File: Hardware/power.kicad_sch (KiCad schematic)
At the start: 13 parts, among them J3 USB_C_Receptacle, U2 ADP2164ACPZ-3.3-R7

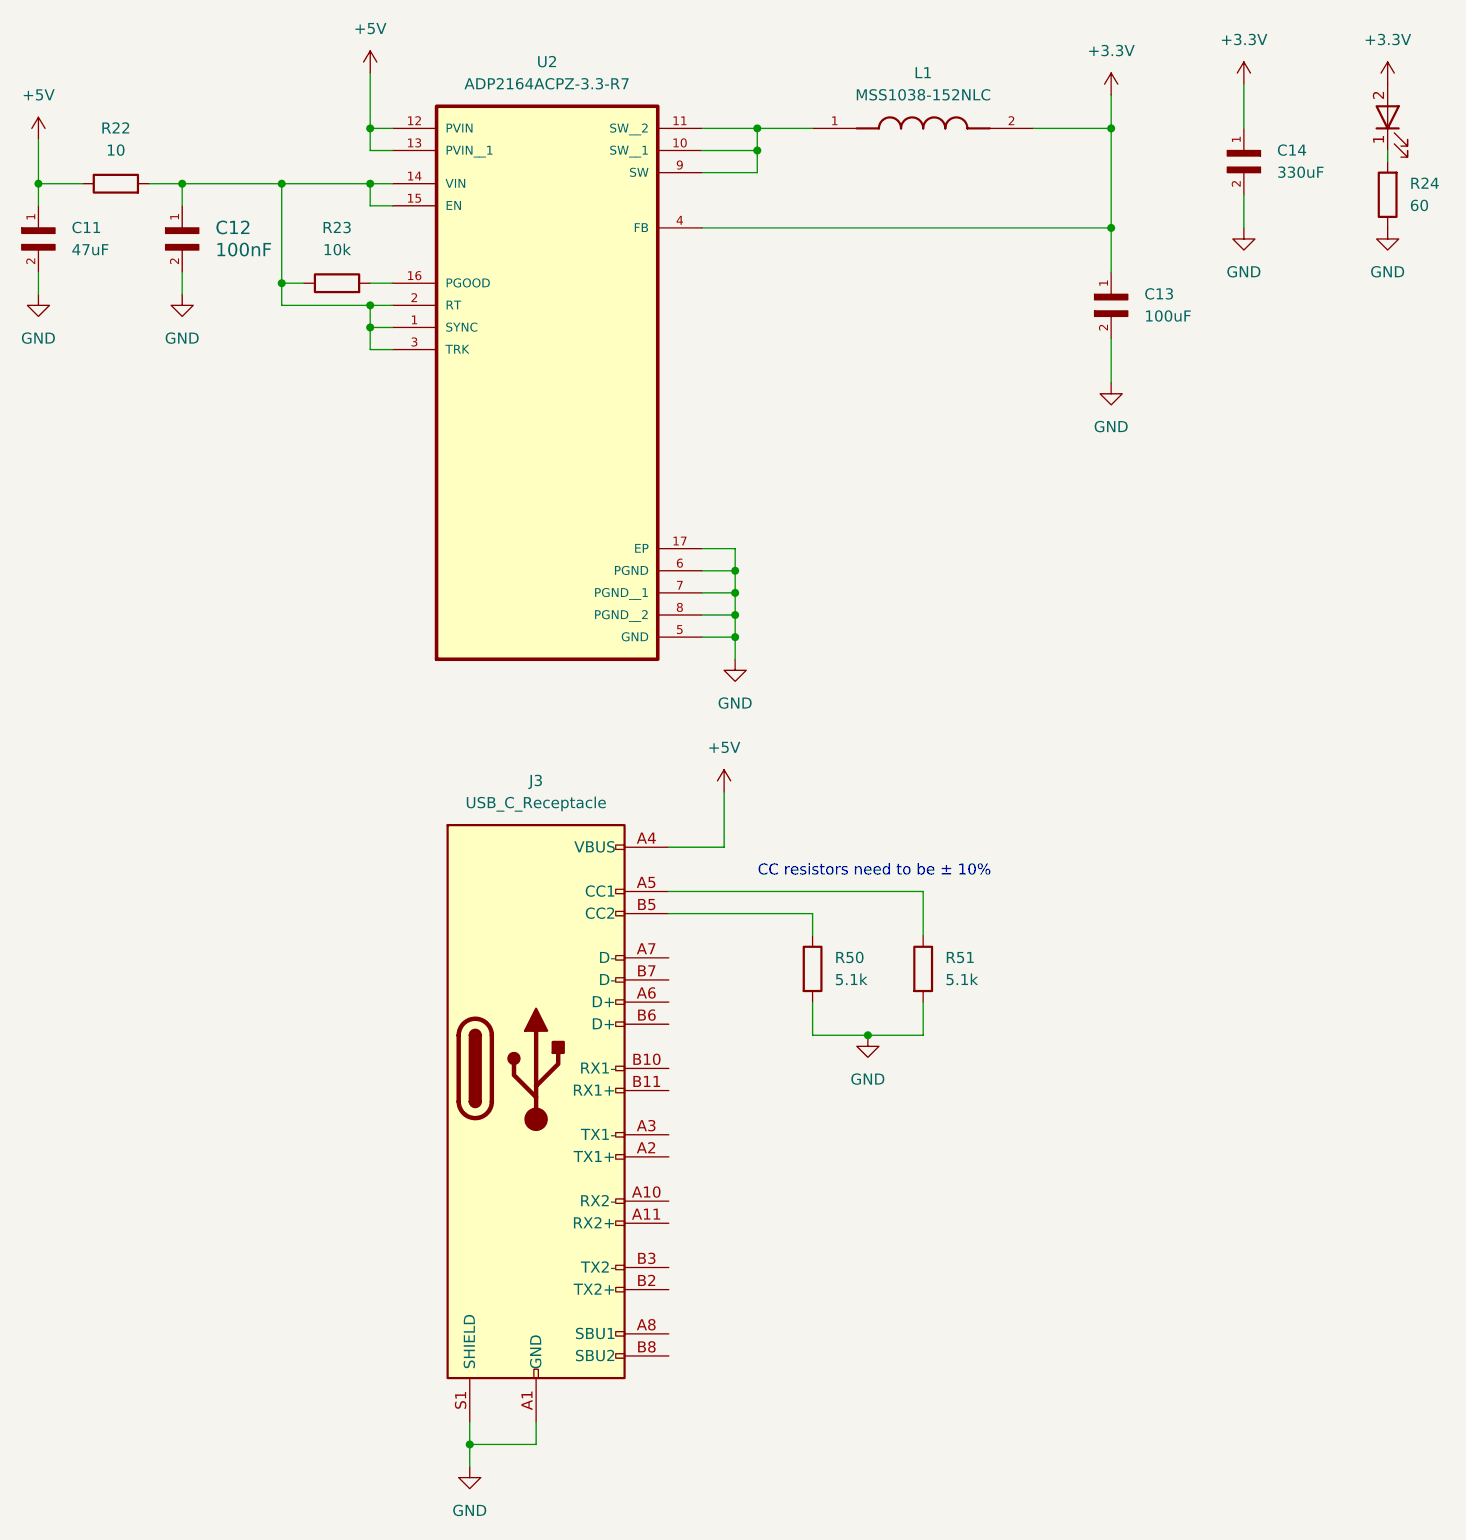
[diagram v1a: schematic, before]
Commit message: changed to SI4468, added 30 MHz oscillators, and connected it to MCU
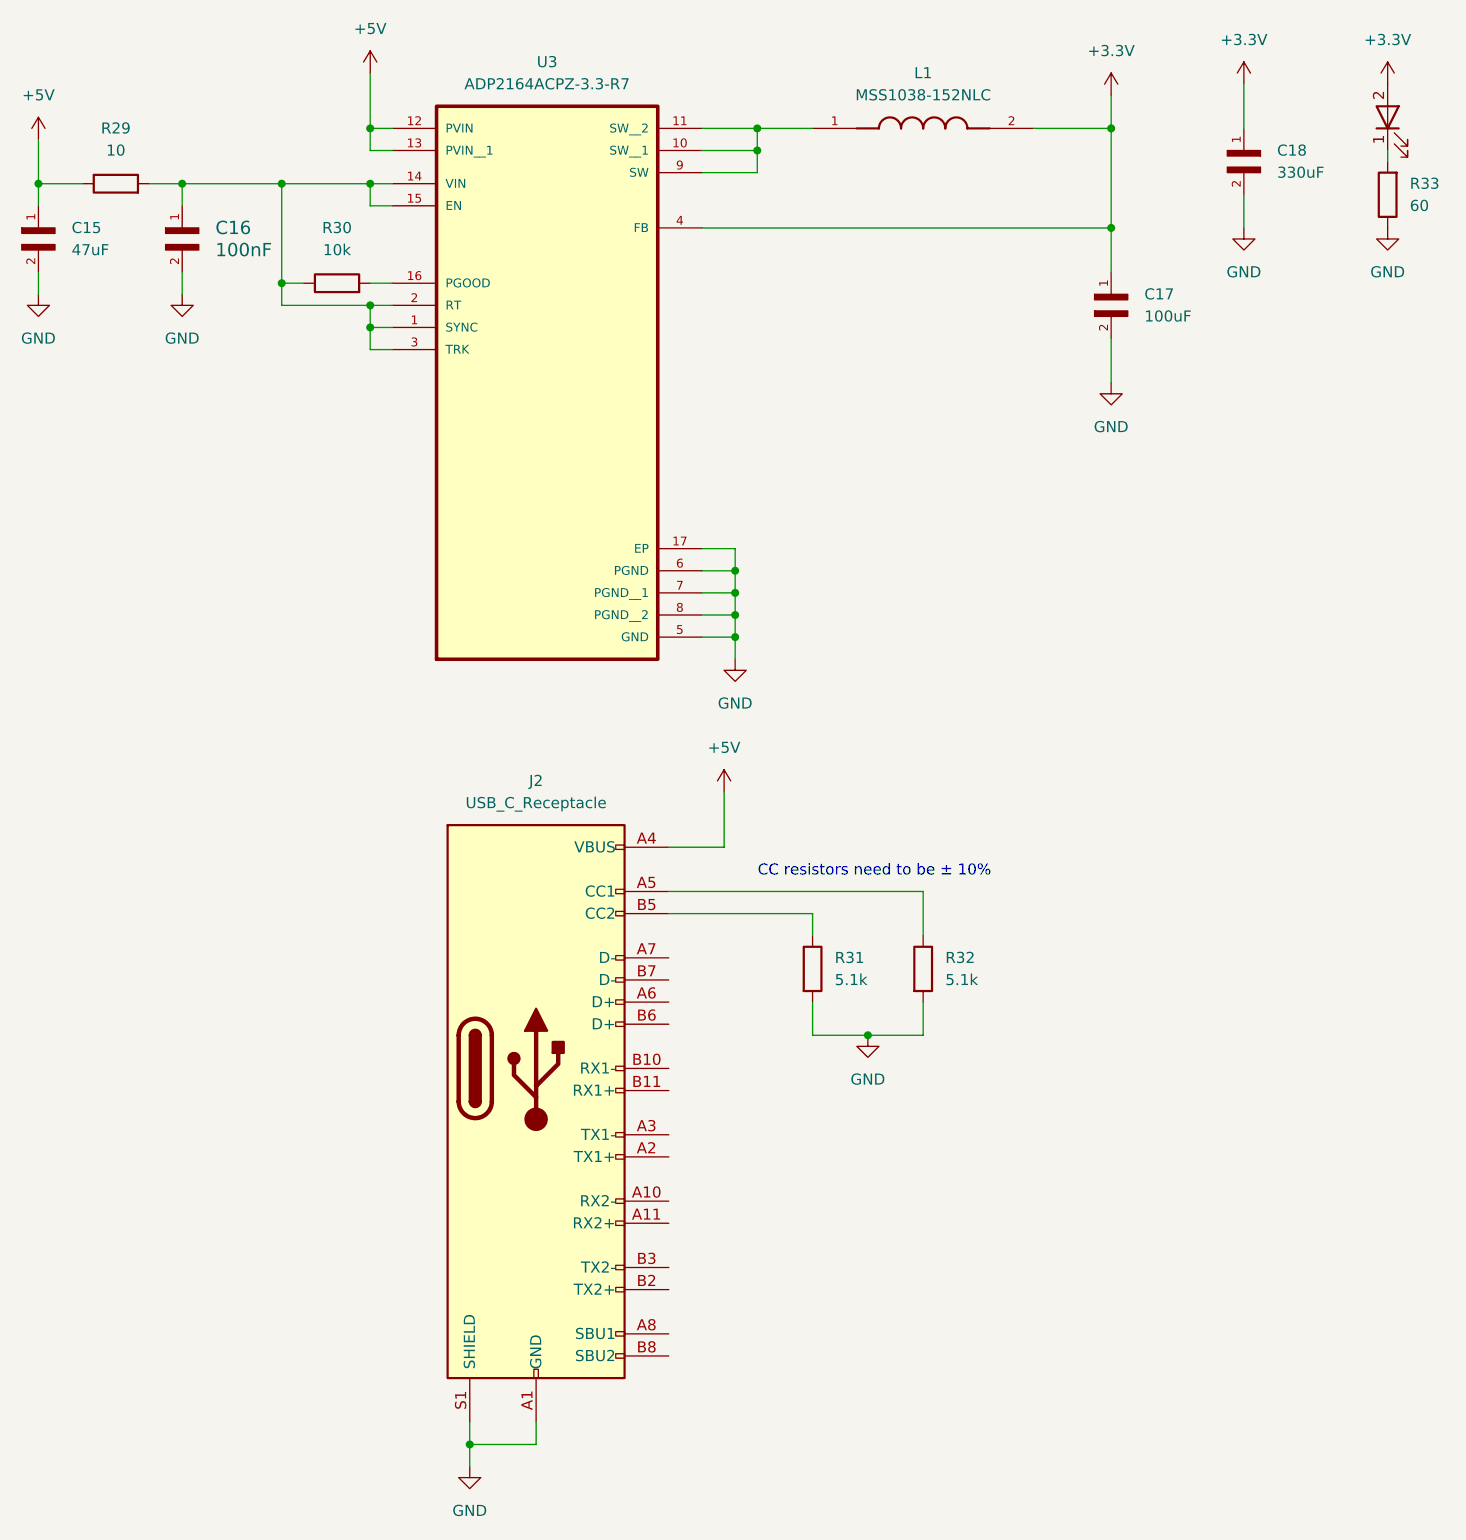
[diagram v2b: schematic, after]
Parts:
- renumbered C11 to C15, C12 to C16, C13 to C17, C14 to C18, J3 to J2, R22 to R29, R23 to R30, R50 to R31, R51 to R32, R24 to R33, U2 to U3
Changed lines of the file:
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@@
 		(dnp no)
 		(fields_autoplaced yes)
-		(property "Reference" "C14"
+		(property "Reference" "C18"
 			(at 170.18 36.8299 90)
 			(effects
@@
 			(project ""
 				(path "/ca6389fe-9846-40e3-87a4-456cfcfc0777/bd0f5978-e4b1-41e2-96b4-94a3773ac12f"
-					(reference "C14")
+					(reference "C18")
 					(unit 1)
 				)
@@
 		(dnp no)
 		(fields_autoplaced yes)
-		(property "Reference" "R22"
+		(property "Reference" "R29"
 			(at 36.83 34.29 90)
 			(effects
@@
 			(project "Radio Project"
 				(path "/ca6389fe-9846-40e3-87a4-456cfcfc0777/bd0f5978-e4b1-41e2-96b4-94a3773ac12f"
-					(reference "R22")
+					(reference "R29")
 					(unit 1)
 				)
@@
 		(dnp no)
 		(fields_autoplaced yes)
-		(property "Reference" "#PWR030"
+		(property "Reference" "#PWR023"
 			(at 77.47 194.31 0)
 			(effects
@@
 			(project "Radio Project"
 				(path "/ca6389fe-9846-40e3-87a4-456cfcfc0777/bd0f5978-e4b1-41e2-96b4-94a3773ac12f"
-					(reference "#PWR030")
+					(reference "#PWR023")
 					(unit 1)
 				)
@@
 		(dnp no)
 		(fields_autoplaced yes)
-		(property "Reference" "#PWR016"
+		(property "Reference" "#PWR027"
 			(at 151.13 34.29 0)
 			(effects
@@
 			(project "Radio Project"
 				(path "/ca6389fe-9846-40e3-87a4-456cfcfc0777/bd0f5978-e4b1-41e2-96b4-94a3773ac12f"
-					(reference "#PWR016")
+					(reference "#PWR027")
 					(unit 1)
 				)
@@
 		(dnp no)
 		(fields_autoplaced yes)
-		(property "Reference" "#PWR031"
+		(property "Reference" "#PWR024"
 			(at 106.68 114.3 0)
 			(effects
@@
 			(project "Radio Project"
 				(path "/ca6389fe-9846-40e3-87a4-456cfcfc0777/bd0f5978-e4b1-41e2-96b4-94a3773ac12f"
-					(reference "#PWR031")
+					(reference "#PWR024")
 					(unit 1)
 				)
@@
 		(dnp no)
 		(fields_autoplaced yes)
-		(property "Reference" "#PWR011"
+		(property "Reference" "#PWR019"
 			(at 27.94 39.37 0)
 			(effects
@@
 			(project "Radio Project"
 				(path "/ca6389fe-9846-40e3-87a4-456cfcfc0777/bd0f5978-e4b1-41e2-96b4-94a3773ac12f"
-					(reference "#PWR011")
+					(reference "#PWR019")
 					(unit 1)
 				)
@@
 		(dnp no)
 		(fields_autoplaced yes)
-		(property "Reference" "R24"
+		(property "Reference" "R33"
 			(at 185.42 40.6399 0)
 			(effects
@@
 			(project "Radio Project"
 				(path "/ca6389fe-9846-40e3-87a4-456cfcfc0777/bd0f5978-e4b1-41e2-96b4-94a3773ac12f"
-					(reference "R24")
+					(reference "R33")
 					(unit 1)
 				)
@@
 		(dnp no)
 		(fields_autoplaced yes)
-		(property "Reference" "#PWR018"
+		(property "Reference" "#PWR029"
 			(at 166.37 33.02 0)
 			(effects
@@
 			(project "Radio Project"
 				(path "/ca6389fe-9846-40e3-87a4-456cfcfc0777/bd0f5978-e4b1-41e2-96b4-94a3773ac12f"
-					(reference "#PWR018")
+					(reference "#PWR029")
 					(unit 1)
 				)
@@
 		(dnp no)
 		(fields_autoplaced yes)
-		(property "Reference" "#PWR015"
+		(property "Reference" "#PWR025"
 			(at 107.95 101.6 0)
 			(effects
@@
 			(project ""
 				(path "/ca6389fe-9846-40e3-87a4-456cfcfc0777/bd0f5978-e4b1-41e2-96b4-94a3773ac12f"
-					(reference "#PWR015")
+					(reference "#PWR025")
 					(unit 1)
 				)
@@
 		(dnp no)
 		(fields_autoplaced yes)
-		(property "Reference" "#PWR044"
+		(property "Reference" "#PWR026"
 			(at 123.19 144.78 0)
 			(effects
@@
 			(project "Radio Project"
 				(path "/ca6389fe-9846-40e3-87a4-456cfcfc0777/bd0f5978-e4b1-41e2-96b4-94a3773ac12f"
-					(reference "#PWR044")
+					(reference "#PWR026")
 					(unit 1)
 				)
@@
 		(dnp no)
 		(fields_autoplaced yes)
-		(property "Reference" "R50"
+		(property "Reference" "R31"
 			(at 119.38 129.5399 0)
 			(effects
@@
 			(project "Radio Project"
 				(path "/ca6389fe-9846-40e3-87a4-456cfcfc0777/bd0f5978-e4b1-41e2-96b4-94a3773ac12f"
-					(reference "R50")
+					(reference "R31")
 					(unit 1)
 				)
@@
 		(dnp no)
 		(fields_autoplaced yes)
-		(property "Reference" "#PWR020"
+		(property "Reference" "#PWR031"
 			(at 182.88 33.02 0)
 			(effects
@@
 			(project "Radio Project"
 				(path "/ca6389fe-9846-40e3-87a4-456cfcfc0777/bd0f5978-e4b1-41e2-96b4-94a3773ac12f"
-					(reference "#PWR020")
+					(reference "#PWR031")
 					(unit 1)
 				)
@@
 		(dnp no)
 		(fields_autoplaced yes)
-		(property "Reference" "J3"
+		(property "Reference" "J2"
 			(at 85.09 109.22 0)
 			(effects
@@
 			(project "Radio Project"
 				(path "/ca6389fe-9846-40e3-87a4-456cfcfc0777/bd0f5978-e4b1-41e2-96b4-94a3773ac12f"
-					(reference "J3")
+					(reference "J2")
 					(unit 1)
 				)
@@
 		(dnp no)
 		(fields_autoplaced yes)
-		(property "Reference" "C13"
+		(property "Reference" "C17"
 			(at 154.94 53.3399 90)
 			(effects
@@
 			(project ""
 				(path "/ca6389fe-9846-40e3-87a4-456cfcfc0777/bd0f5978-e4b1-41e2-96b4-94a3773ac12f"
-					(reference "C13")
+					(reference "C17")
 					(unit 1)
 				)
@@
 		(dnp no)
 		(fields_autoplaced yes)
-		(property "Reference" "#PWR017"
+		(property "Reference" "#PWR028"
 			(at 151.13 69.85 0)
 			(effects
@@
 			(project "Radio Project"
 				(path "/ca6389fe-9846-40e3-87a4-456cfcfc0777/bd0f5978-e4b1-41e2-96b4-94a3773ac12f"
-					(reference "#PWR017")
+					(reference "#PWR028")
 					(unit 1)
 				)
@@
 		(dnp no)
 		(fields_autoplaced yes)
-		(property "Reference" "C12"
+		(property "Reference" "C16"
 			(at 48.26 45.7199 90)
 			(effects
@@
 			(project ""
 				(path "/ca6389fe-9846-40e3-87a4-456cfcfc0777/bd0f5978-e4b1-41e2-96b4-94a3773ac12f"
-					(reference "C12")
+					(reference "C16")
 					(unit 1)
 				)
@@
 		(dnp no)
 		(fields_autoplaced yes)
-		(property "Reference" "#PWR013"
+		(property "Reference" "#PWR021"
 			(at 44.45 59.69 0)
 			(effects
@@
 			(project "Radio Project"
 				(path "/ca6389fe-9846-40e3-87a4-456cfcfc0777/bd0f5978-e4b1-41e2-96b4-94a3773ac12f"
-					(reference "#PWR013")
+					(reference "#PWR021")
 					(unit 1)
 				)
@@
 		(dnp no)
 		(fields_autoplaced yes)
-		(property "Reference" "C11"
+		(property "Reference" "C15"
 			(at 31.75 45.7199 90)
 			(effects
@@
 			(project ""
 				(path "/ca6389fe-9846-40e3-87a4-456cfcfc0777/bd0f5978-e4b1-41e2-96b4-94a3773ac12f"
-					(reference "C11")
+					(reference "C15")
 					(unit 1)
 				)
@@
 		(dnp no)
 		(fields_autoplaced yes)
-		(property "Reference" "#PWR021"
+		(property "Reference" "#PWR032"
 			(at 182.88 52.07 0)
 			(effects
@@
 			(project "Radio Project"
 				(path "/ca6389fe-9846-40e3-87a4-456cfcfc0777/bd0f5978-e4b1-41e2-96b4-94a3773ac12f"
-					(reference "#PWR021")
+					(reference "#PWR032")
 					(unit 1)
 				)
@@
 		(dnp no)
 		(fields_autoplaced yes)
-		(property "Reference" "#PWR014"
+		(property "Reference" "#PWR022"
 			(at 66.04 31.75 0)
 			(effects
@@
 			(project ""
 				(path "/ca6389fe-9846-40e3-87a4-456cfcfc0777/bd0f5978-e4b1-41e2-96b4-94a3773ac12f"
-					(reference "#PWR014")
+					(reference "#PWR022")
 					(unit 1)
 				)
@@
 		(dnp no)
 		(fields_autoplaced yes)
-		(property "Reference" "#PWR012"
+		(property "Reference" "#PWR020"
 			(at 27.94 59.69 0)
 			(effects
@@
 			(project "Radio Project"
 				(path "/ca6389fe-9846-40e3-87a4-456cfcfc0777/bd0f5978-e4b1-41e2-96b4-94a3773ac12f"
-					(reference "#PWR012")
+					(reference "#PWR020")
 					(unit 1)
 				)
@@
 		(dnp no)
 		(fields_autoplaced yes)
-		(property "Reference" "U2"
+		(property "Reference" "U3"
 			(at 86.36 26.67 0)
 			(effects
@@
 			(project ""
 				(path "/ca6389fe-9846-40e3-87a4-456cfcfc0777/bd0f5978-e4b1-41e2-96b4-94a3773ac12f"
-					(reference "U2")
+					(reference "U3")
 					(unit 1)
 				)
@@
 		(dnp no)
 		(fields_autoplaced yes)
-		(property "Reference" "R23"
+		(property "Reference" "R30"
 			(at 62.23 45.72 90)
 			(effects
@@
 			(project "Radio Project"
 				(path "/ca6389fe-9846-40e3-87a4-456cfcfc0777/bd0f5978-e4b1-41e2-96b4-94a3773ac12f"
-					(reference "R23")
+					(reference "R30")
 					(unit 1)
 				)
@@
 		(dnp no)
 		(fields_autoplaced yes)
-		(property "Reference" "R51"
+		(property "Reference" "R32"
 			(at 132.08 129.5399 0)
 			(effects
@@
 			(project "Radio Project"
 				(path "/ca6389fe-9846-40e3-87a4-456cfcfc0777/bd0f5978-e4b1-41e2-96b4-94a3773ac12f"
-					(reference "R51")
+					(reference "R32")
 					(unit 1)
 				)
@@
 		(dnp no)
 		(fields_autoplaced yes)
-		(property "Reference" "#PWR019"
+		(property "Reference" "#PWR030"
 			(at 166.37 52.07 0)
 			(effects
@@
 			(project "Radio Project"
 				(path "/ca6389fe-9846-40e3-87a4-456cfcfc0777/bd0f5978-e4b1-41e2-96b4-94a3773ac12f"
-					(reference "#PWR019")
-					(unit 1)
-				)
+					(reference "#PWR030")
+					(unit 1)
+				)
